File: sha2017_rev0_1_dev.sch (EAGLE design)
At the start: 82 parts, among them IC1 CP210X_USB_UART, IC2 AP7215, IC32 ESP32_AI, Q1 MMBT2222A, Q2 MMBT2222A, Q6 MOSFET-NCHANNELBSS123LT1G, SW801 MCMT5-F-V, X701 2908-05WB-MG

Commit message: initial PCB design
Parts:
- C11: device rcl:C-EUC0603 -> rcl:C-EUC0805
- C12, C15, C16, C26, C27: device 00ralf:C0603-DASHES -> rcl:C-EUC0805
- L1: device SparkFun-Passives:INDUCTOR- -> SparkFun-Passives:INDUCTOR1210
- R714: device rcl:R-EU_R0402 -> rcl:R-EU_R0603
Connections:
- removed net SD_DAT0: X701.DO
- removed net SD_DAT1: X701.RSV
- removed net SD_DAT2: X701.NC
- removed net SD_DAT3: X701.CS
- net SD_DATA0: now also X701.DO
- net SD_DATA1: now also X701.RSV
- net SD_DATA2: now also X701.NC
- net SD_DATA3: now also X701.CS
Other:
- moved on the sheet: C27
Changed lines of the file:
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@@
 <setting verticaltext="up"/>
 </settings>
-<grid distance="0.1" unitdist="inch" unit="inch" style="lines" multiple="1" display="no" altdistance="0.01" altunitdist="inch" altunit="inch"/>
+<grid distance="0.05" unitdist="inch" unit="inch" style="lines" multiple="1" display="no" altdistance="0.01" altunitdist="inch" altunit="inch"/>
 <layers>
 <layer number="1" name="Top" color="4" fill="1" visible="no" active="no"/>
@@
 <part name="USB100" library="usb_con-update" deviceset="MOLEX-47346-0001" device=""/>
 <part name="GND47" library="supply1" deviceset="GND" device=""/>
-<part name="C27" library="00ralf" deviceset="C0603-DASHES" device="" value="2u2/16V"/>
+<part name="C27" library="rcl" deviceset="C-EU" device="C0805" value="2u2/16V"/>
 <part name="GND46" library="supply1" deviceset="GND" device=""/>
 <part name="F1" library="SparkFun-PowerIC" deviceset="PTC" device="SMD" value="500mA"/>
@@
 <part name="D11" library="SparkFun-DiscreteSemi" deviceset="BAT20JFILM" device="" value="NSVR0320MW2T1G"/>
 <part name="C10" library="00ralf" deviceset="C0603-DASHES" device="" value="4u7/16V"/>
-<part name="C11" library="rcl" deviceset="C-EU" device="C0603" value="100n"/>
-<part name="C12" library="00ralf" deviceset="C0603-DASHES" device="" value="4u7/16V"/>
+<part name="C11" library="rcl" deviceset="C-EU" device="C0805" value="100n"/>
+<part name="C12" library="rcl" deviceset="C-EU" device="C0805" value="4u7/16V"/>
 <part name="C13" library="00ralf" deviceset="C0603-DASHES" device="" value="4u7/16V"/>
 <part name="C14" library="rcl" deviceset="C-EU" device="C0603" value="100n"/>
@@
 <part name="GND27" library="supply1" deviceset="GND" device=""/>
 <part name="+3V2" library="supply1" deviceset="+3V3" device=""/>
-<part name="C15" library="00ralf" deviceset="C0603-DASHES" device="" value="4u7/16V"/>
-<part name="C16" library="00ralf" deviceset="C0603-DASHES" device="" value="4u7/16V"/>
+<part name="C15" library="rcl" deviceset="C-EU" device="C0805" value="4u7/16V"/>
+<part name="C16" library="rcl" deviceset="C-EU" device="C0805" value="4u7/16V"/>
 <part name="GND28" library="supply1" deviceset="GND" device=""/>
 <part name="GND29" library="supply1" deviceset="GND" device=""/>
@@
 <part name="+3V1" library="supply1" deviceset="+3V3" device=""/>
 <part name="C25" library="00ralf" deviceset="C0603-DASHES" device="" value="1u"/>
-<part name="L1" library="SparkFun-Passives" deviceset="INDUCTOR" device="-" value="22µ"/>
-<part name="C26" library="00ralf" deviceset="C0603-DASHES" device="" value="4u7/16V"/>
+<part name="L1" library="SparkFun-Passives" deviceset="INDUCTOR" device="1210" value="22µ"/>
+<part name="C26" library="rcl" deviceset="C-EU" device="C0805" value="4u7/16V"/>
 <part name="+3V3" library="supply1" deviceset="+3V3" device=""/>
 <part name="GND37" library="supply1" deviceset="GND" device=""/>
@@
 <part name="GND59" library="supply1" deviceset="GND" device=""/>
 <part name="P+14" library="supply1" deviceset="VCC" device=""/>
-<part name="R714" library="rcl" deviceset="R-EU_" device="R0402" value="100k"/>
+<part name="R714" library="rcl" deviceset="R-EU_" device="R0603" value="100k"/>
 <part name="D2" library="SparkFun-LED" deviceset="LED" device="0603"/>
 <part name="D4" library="SparkFun-LED" deviceset="LED" device="0603"/>
@@
 <instance part="C25" gate="G$1" x="314.96" y="171.45" rot="MR0"/>
 <instance part="L1" gate="G$1" x="264.16" y="175.26" rot="R90"/>
-<instance part="C26" gate="G$1" x="256.54" y="171.45" rot="MR0"/>
+<instance part="C26" gate="G$1" x="256.54" y="172.72" rot="MR0"/>
 <instance part="+3V3" gate="G$1" x="246.38" y="175.26" rot="R90"/>
 <instance part="GND37" gate="1" x="256.54" y="165.1"/>
@@
 <segment>
 <pinref part="GND46" gate="1" pin="GND"/>
-<wire x1="76.2" y1="172.72" x2="76.2" y2="176.53" width="0.1524" layer="91"/>
+<wire x1="76.2" y1="172.72" x2="76.2" y2="175.26" width="0.1524" layer="91"/>
 <pinref part="C27" gate="G$1" pin="2"/>
 </segment>
@@
 <pinref part="C27" gate="G$1" pin="1"/>
 <wire x1="73.66" y1="193.04" x2="76.2" y2="193.04" width="0.1524" layer="91"/>
-<wire x1="76.2" y1="184.15" x2="76.2" y2="193.04" width="0.1524" layer="91"/>
+<wire x1="76.2" y1="182.88" x2="76.2" y2="193.04" width="0.1524" layer="91"/>
 <junction x="76.2" y="193.04"/>
 <pinref part="F1" gate="G$1" pin="2"/>
@@
 </segment>
 </net>
-<net name="SD_DAT2" class="0">
+<net name="SD_DATA2" class="0">
 <segment>
 <pinref part="X701" gate="G$1" pin="NC"/>
@@
 </segment>
 </net>
-<net name="SD_DAT0" class="0">
+<net name="SD_DATA0" class="0">
 <segment>
 <pinref part="X701" gate="G$1" pin="DO"/>
@@
 </segment>
 </net>
-<net name="SD_DAT1" class="0">
+<net name="SD_DATA1" class="0">
 <segment>
 <pinref part="X701" gate="G$1" pin="RSV"/>
@@
 </segment>
 </net>
-<net name="SD_DAT3" class="0">
+<net name="SD_DATA3" class="0">
 <segment>
 <pinref part="X701" gate="G$1" pin="CS"/>
@@
 <instance part="C10" gate="G$1" x="137.16" y="135.89" rot="MR0"/>
 <instance part="C11" gate="G$1" x="132.08" y="137.16"/>
-<instance part="C12" gate="G$1" x="187.96" y="135.89" rot="MR0"/>
+<instance part="C12" gate="G$1" x="187.96" y="137.16" rot="MR0"/>
 <instance part="C13" gate="G$1" x="193.04" y="135.89" rot="MR0"/>
 <instance part="C14" gate="G$1" x="198.12" y="137.16"/>
@@
 <instance part="GND27" gate="1" x="198.12" y="129.54" rot="MR0"/>
 <instance part="+3V2" gate="G$1" x="208.28" y="139.7" rot="R270"/>
-<instance part="C15" gate="G$1" x="182.88" y="135.89" rot="MR0"/>
-<instance part="C16" gate="G$1" x="177.8" y="135.89" rot="MR0"/>
+<instance part="C15" gate="G$1" x="182.88" y="137.16" rot="MR0"/>
+<instance part="C16" gate="G$1" x="177.8" y="137.16" rot="MR0"/>
 <instance part="GND28" gate="1" x="182.88" y="129.54" rot="MR0"/>
 <instance part="GND29" gate="1" x="177.8" y="129.54" rot="MR0"/>

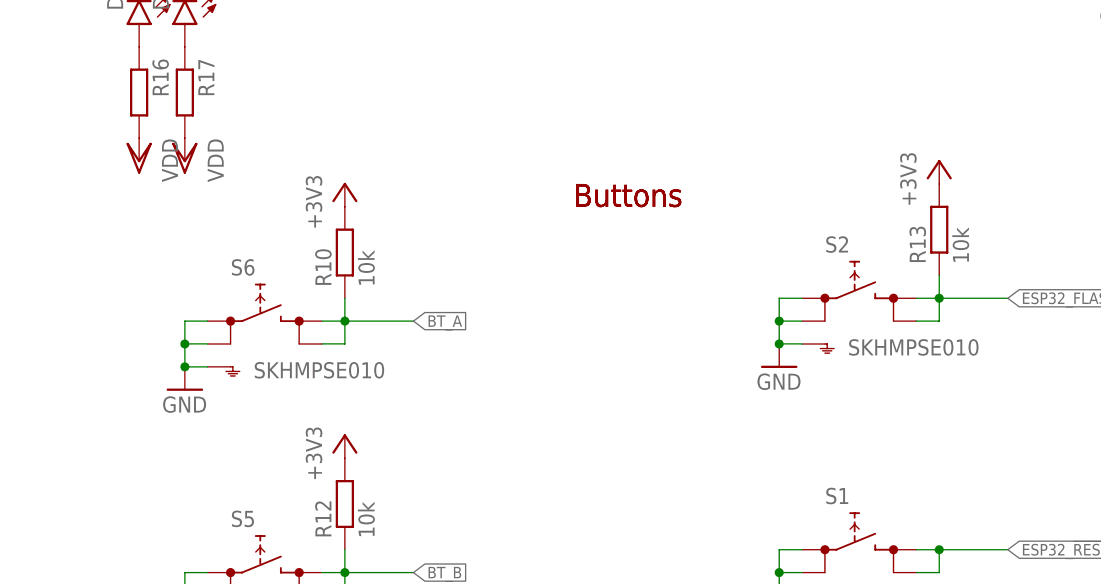
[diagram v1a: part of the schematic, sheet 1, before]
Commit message: removed dedicated flash switch, switch A will be now flash and switch A.
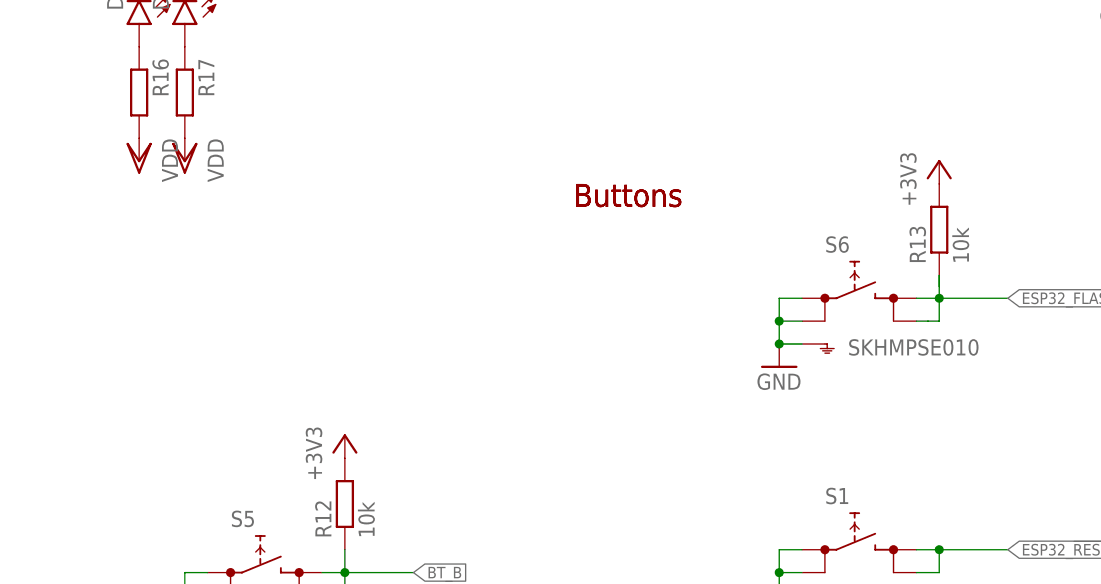
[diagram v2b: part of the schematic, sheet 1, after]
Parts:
- removed R10: 10k, rcl:R-EU_R0603
- removed S2: SKHMPSE010, switch:SKHMPSE010
- removed SJ1: JUMPER-PAD-2-NC_BY_TRACE, SparkFun-Passives:JUMPER-PAD-2-NC_BY_TRACE
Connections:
- removed net BT_A: R10.1, S6.2.1, S6.2.2, SJ1.1
- net +3V3: no longer R10.2
- net ESP32_FLASH/TOUCHE_MENU: now also S6.2.1, S6.2.2; no longer S2.2.1, S2.2.2
- net GND: no longer S2.1.1, S2.1.2, S2.SH
- net N$15: no longer SJ1.2
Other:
- moved on the sheet: S6
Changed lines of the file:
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@@
 <setting verticaltext="up"/>
 </settings>
-<grid distance="0.05" unitdist="inch" unit="inch" style="lines" multiple="1" display="no" altdistance="0.01" altunitdist="inch" altunit="inch"/>
+<grid distance="0.1" unitdist="inch" unit="inch" style="lines" multiple="1" display="no" altdistance="0.01" altunitdist="inch" altunit="inch"/>
 <layers>
 <layer number="1" name="Top" color="4" fill="1" visible="no" active="no"/>
@@
 <part name="S6" library="switch" deviceset="SKHMP*E010" device="" technology="S"/>
 <part name="GND12" library="supply1" deviceset="GND" device=""/>
-<part name="R10" library="rcl" deviceset="R-EU_" device="R0603" value="10k"/>
 <part name="R12" library="rcl" deviceset="R-EU_" device="R0603" value="10k"/>
-<part name="+3V7" library="supply1" deviceset="+3V3" device=""/>
 <part name="+3V8" library="supply1" deviceset="+3V3" device=""/>
-<part name="SJ1" library="SparkFun-Passives" deviceset="JUMPER-PAD-2-NC_BY_TRACE" device=""/>
 <part name="SJ2" library="SparkFun-Passives" deviceset="JUMPER-PAD-2-NC_BY_TRACE" device=""/>
 <part name="SJ3" library="SparkFun-Passives" deviceset="JUMPER-PAD-2-NC_BY_TRACE" device=""/>
@@
 <part name="S1" library="switch" deviceset="SKHMP*E010" device="" technology="S"/>
 <part name="GND13" library="supply1" deviceset="GND" device=""/>
-<part name="S2" library="switch" deviceset="SKHMP*E010" device="" technology="S"/>
-<part name="GND14" library="supply1" deviceset="GND" device=""/>
 <part name="R13" library="rcl" deviceset="R-EU_" device="R0603" value="10k"/>
 <part name="+3V10" library="supply1" deviceset="+3V3" device=""/>
@@
 <instance part="S5" gate="G$1" x="160.02" y="101.6"/>
 <instance part="GND11" gate="1" x="152.4" y="93.98"/>
-<instance part="S6" gate="G$1" x="160.02" y="129.54"/>
-<instance part="GND12" gate="1" x="152.4" y="121.92"/>
-<instance part="R10" gate="G$1" x="170.18" y="137.16" rot="R90"/>
+<instance part="S6" gate="G$1" x="226.06" y="132.08"/>
+<instance part="GND12" gate="1" x="218.44" y="124.46"/>
 <instance part="R12" gate="G$1" x="170.18" y="109.22" rot="R90"/>
-<instance part="+3V7" gate="G$1" x="170.18" y="144.78"/>
 <instance part="+3V8" gate="G$1" x="170.18" y="116.84"/>
 <instance part="S1" gate="G$1" x="226.06" y="104.14"/>
 <instance part="GND13" gate="1" x="218.44" y="96.52"/>
-<instance part="S2" gate="G$1" x="226.06" y="132.08"/>
-<instance part="GND14" gate="1" x="218.44" y="124.46"/>
 <instance part="R13" gate="G$1" x="236.22" y="139.7" rot="R90"/>
 <instance part="+3V10" gate="G$1" x="236.22" y="147.32"/>
@@
 <segment>
 <pinref part="S6" gate="G$1" pin="1.1"/>
-<wire x1="154.94" y1="129.54" x2="152.4" y2="129.54" width="0.1524" layer="91"/>
-<wire x1="152.4" y1="129.54" x2="152.4" y2="127" width="0.1524" layer="91"/>
+<wire x1="220.98" y1="132.08" x2="218.44" y2="132.08" width="0.1524" layer="91"/>
+<wire x1="218.44" y1="132.08" x2="218.44" y2="129.54" width="0.1524" layer="91"/>
 <pinref part="S6" gate="G$1" pin="SH"/>
-<wire x1="152.4" y1="127" x2="152.4" y2="124.46" width="0.1524" layer="91"/>
-<wire x1="152.4" y1="124.46" x2="154.94" y2="124.46" width="0.1524" layer="91"/>
+<wire x1="218.44" y1="129.54" x2="218.44" y2="127" width="0.1524" layer="91"/>
+<wire x1="218.44" y1="127" x2="220.98" y2="127" width="0.1524" layer="91"/>
 <pinref part="S6" gate="G$1" pin="1.2"/>
-<wire x1="154.94" y1="127" x2="152.4" y2="127" width="0.1524" layer="91"/>
+<wire x1="220.98" y1="129.54" x2="218.44" y2="129.54" width="0.1524" layer="91"/>
 <pinref part="GND12" gate="1" pin="GND"/>
-<junction x="152.4" y="124.46"/>
-<junction x="152.4" y="127"/>
+<junction x="218.44" y="127"/>
+<junction x="218.44" y="129.54"/>
 </segment>
 <segment>
@@
 <wire x1="218.44" y1="101.6" x2="218.44" y2="99.06" width="0.1524" layer="91"/>
 <junction x="218.44" y="99.06"/>
-</segment>
-<segment>
-<pinref part="S2" gate="G$1" pin="1.1"/>
-<wire x1="220.98" y1="132.08" x2="218.44" y2="132.08" width="0.1524" layer="91"/>
-<wire x1="218.44" y1="132.08" x2="218.44" y2="129.54" width="0.1524" layer="91"/>
-<pinref part="S2" gate="G$1" pin="SH"/>
-<wire x1="218.44" y1="129.54" x2="218.44" y2="127" width="0.1524" layer="91"/>
-<wire x1="218.44" y1="127" x2="220.98" y2="127" width="0.1524" layer="91"/>
-<pinref part="S2" gate="G$1" pin="1.2"/>
-<wire x1="220.98" y1="129.54" x2="218.44" y2="129.54" width="0.1524" layer="91"/>
-<pinref part="GND14" gate="1" pin="GND"/>
-<junction x="218.44" y="127"/>
-<junction x="218.44" y="129.54"/>
 </segment>
 <segment>
@@
 </segment>
 <segment>
-<pinref part="S2" gate="G$1" pin="2.2"/>
-<wire x1="233.68" y1="129.54" x2="236.22" y2="129.54" width="0.1524" layer="91"/>
+<wire x1="233.68" y1="132.08" x2="236.22" y2="132.08" width="0.1524" layer="91"/>
+<label x="243.84" y="132.08" size="1.27" layer="95" xref="yes"/>
+<pinref part="S6" gate="G$1" pin="2.1"/>
+<pinref part="R13" gate="G$1" pin="1"/>
+<wire x1="236.22" y1="132.08" x2="243.84" y2="132.08" width="0.1524" layer="91"/>
+<wire x1="236.22" y1="133.35" x2="236.22" y2="134.62" width="0.1524" layer="91"/>
+<wire x1="236.22" y1="134.62" x2="236.22" y2="132.08" width="0.1524" layer="91"/>
 <wire x1="236.22" y1="129.54" x2="236.22" y2="132.08" width="0.1524" layer="91"/>
-<pinref part="S2" gate="G$1" pin="2.1"/>
-<wire x1="236.22" y1="132.08" x2="236.22" y2="134.62" width="0.1524" layer="91"/>
-<wire x1="233.68" y1="132.08" x2="236.22" y2="132.08" width="0.1524" layer="91"/>
-<pinref part="R13" gate="G$1" pin="1"/>
+<wire x1="234.95" y1="129.54" x2="236.22" y2="129.54" width="0.1524" layer="91"/>
+<pinref part="S6" gate="G$1" pin="2.2"/>
+<wire x1="233.68" y1="129.54" x2="234.95" y2="129.54" width="0.1524" layer="91"/>
 <junction x="236.22" y="132.08"/>
-<wire x1="236.22" y1="132.08" x2="243.84" y2="132.08" width="0.1524" layer="91"/>
-<label x="243.84" y="132.08" size="1.27" layer="95" xref="yes"/>
 </segment>
 </net>
@@
 </segment>
 <segment>
-<pinref part="R10" gate="G$1" pin="2"/>
-<pinref part="+3V7" gate="G$1" pin="+3V3"/>
-</segment>
-<segment>
 <pinref part="R12" gate="G$1" pin="2"/>
 <pinref part="+3V8" gate="G$1" pin="+3V3"/>
@@
 <wire x1="170.18" y1="101.6" x2="177.8" y2="101.6" width="0.1524" layer="91"/>
 <label x="177.8" y="101.6" size="1.27" layer="95" xref="yes"/>
-</segment>
-</net>
-<net name="BT_A" class="0">
-<segment>
-<pinref part="S6" gate="G$1" pin="2.2"/>
-<wire x1="167.64" y1="127" x2="170.18" y2="127" width="0.1524" layer="91"/>
-<wire x1="170.18" y1="127" x2="170.18" y2="129.54" width="0.1524" layer="91"/>
-<pinref part="S6" gate="G$1" pin="2.1"/>
-<wire x1="170.18" y1="129.54" x2="170.18" y2="132.08" width="0.1524" layer="91"/>
-<wire x1="167.64" y1="129.54" x2="170.18" y2="129.54" width="0.1524" layer="91"/>
-<pinref part="R10" gate="G$1" pin="1"/>
-<junction x="170.18" y="129.54"/>
-<wire x1="170.18" y1="129.54" x2="177.8" y2="129.54" width="0.1524" layer="91"/>
-<label x="177.8" y="129.54" size="1.27" layer="95" xref="yes"/>
 </segment>
 </net>
@@
 <instance part="JP2" gate="G$1" x="210.82" y="160.02" rot="R180"/>
 <instance part="JP3" gate="G$1" x="175.26" y="127" rot="R90"/>
-<instance part="SJ1" gate="G$1" x="129.54" y="162.56" smashed="yes">
-<attribute name="NAME" x="132.08" y="162.56" size="1.778" layer="95"/>
-</instance>
 <instance part="SJ2" gate="G$1" x="121.92" y="160.02" smashed="yes">
 <attribute name="NAME" x="124.46" y="160.02" size="1.778" layer="95"/>
@@
 <pinref part="IC32" gate="G$1" pin="IO34"/>
 <pinref part="JP1" gate="G$1" pin="7"/>
-<wire x1="149.86" y1="162.56" x2="134.62" y2="162.56" width="0.1524" layer="91"/>
-<junction x="149.86" y="162.56"/>
-<pinref part="SJ1" gate="G$1" pin="2"/>
 </segment>
 </net>
@@
 </segment>
 </net>
-<net name="BT_A" class="0">
-<segment>
-<pinref part="SJ1" gate="G$1" pin="1"/>
-<wire x1="124.46" y1="162.56" x2="114.3" y2="162.56" width="0.1524" layer="91"/>
-<label x="114.3" y="162.56" size="1.27" layer="95" rot="R180" xref="yes"/>
-</segment>
-</net>
